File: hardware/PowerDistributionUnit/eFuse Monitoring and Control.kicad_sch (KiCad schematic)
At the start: 103 parts, among them U34 MCP23017_SO, U37 MCP23017_SO, U38 ADS131M08-Q1, U39 ADS131M08-Q1, Y1 ABM3-8.000MHZ-D2Y-T

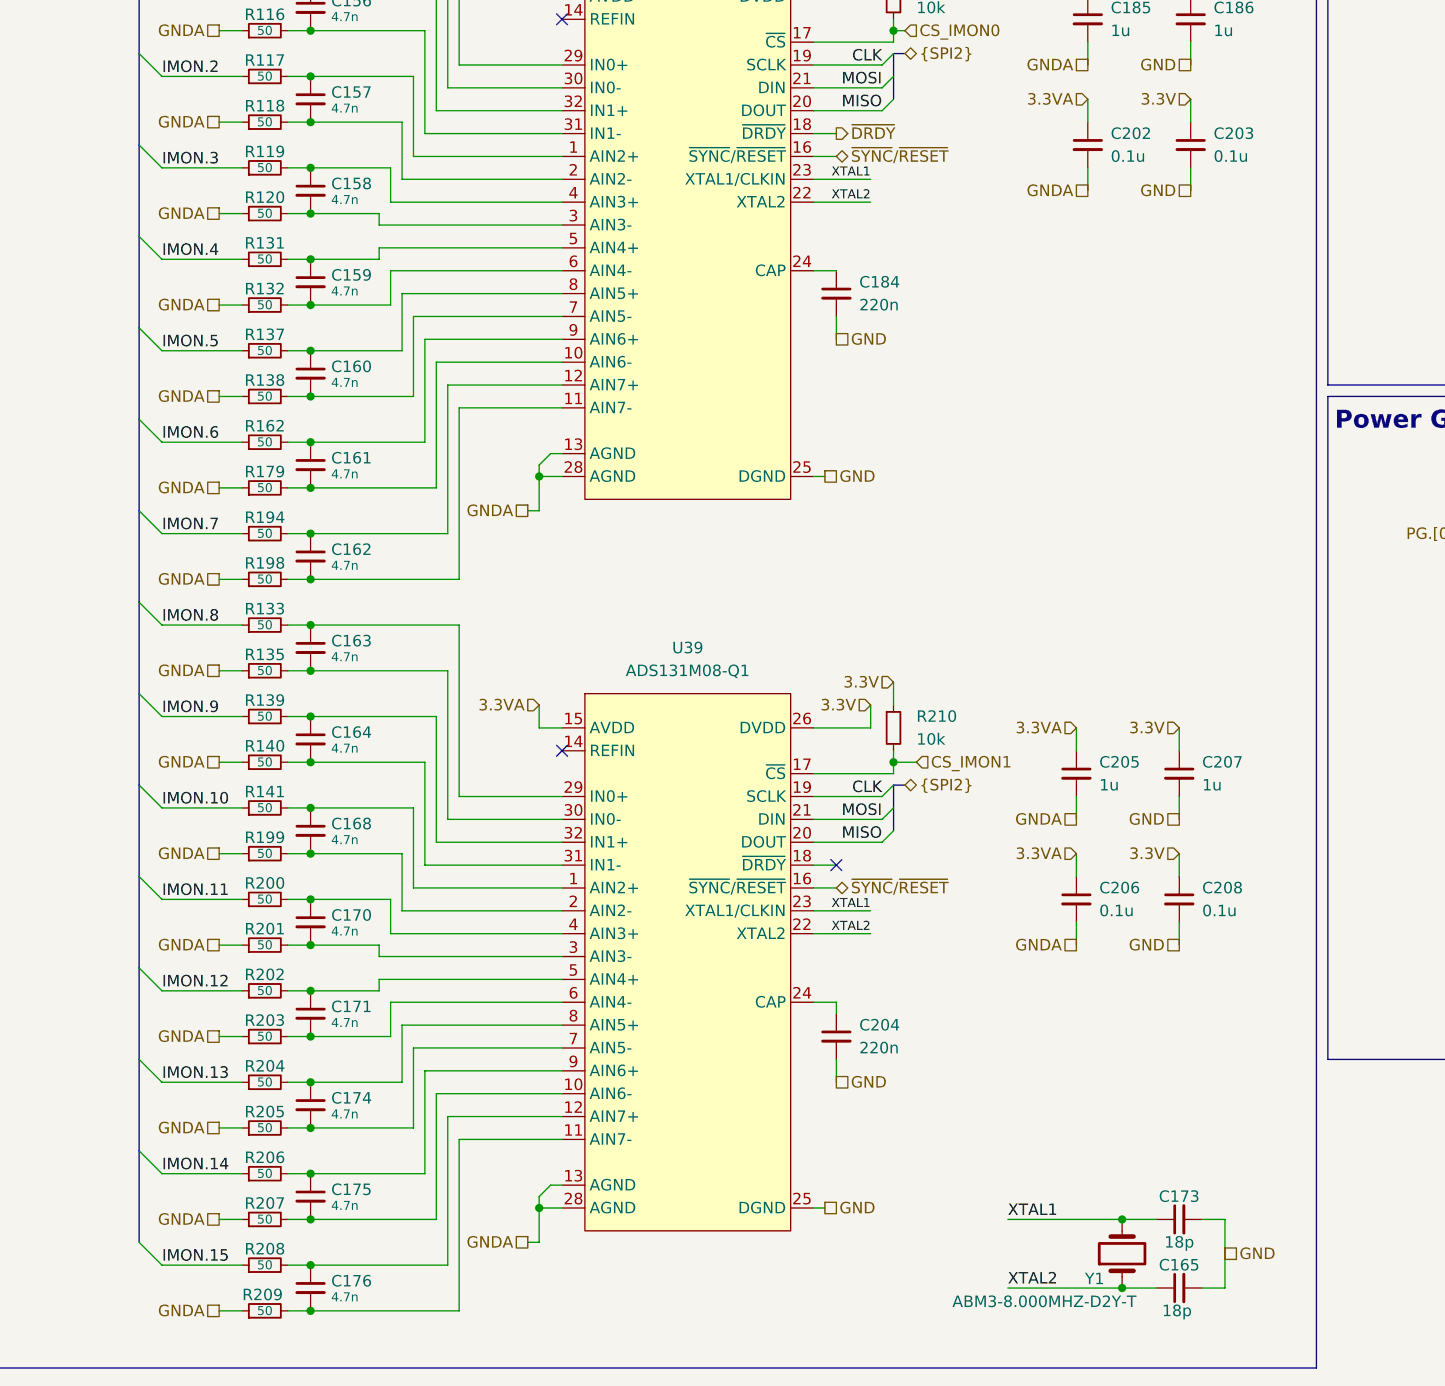
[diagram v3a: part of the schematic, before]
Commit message: updated adc, preliminary routing plan
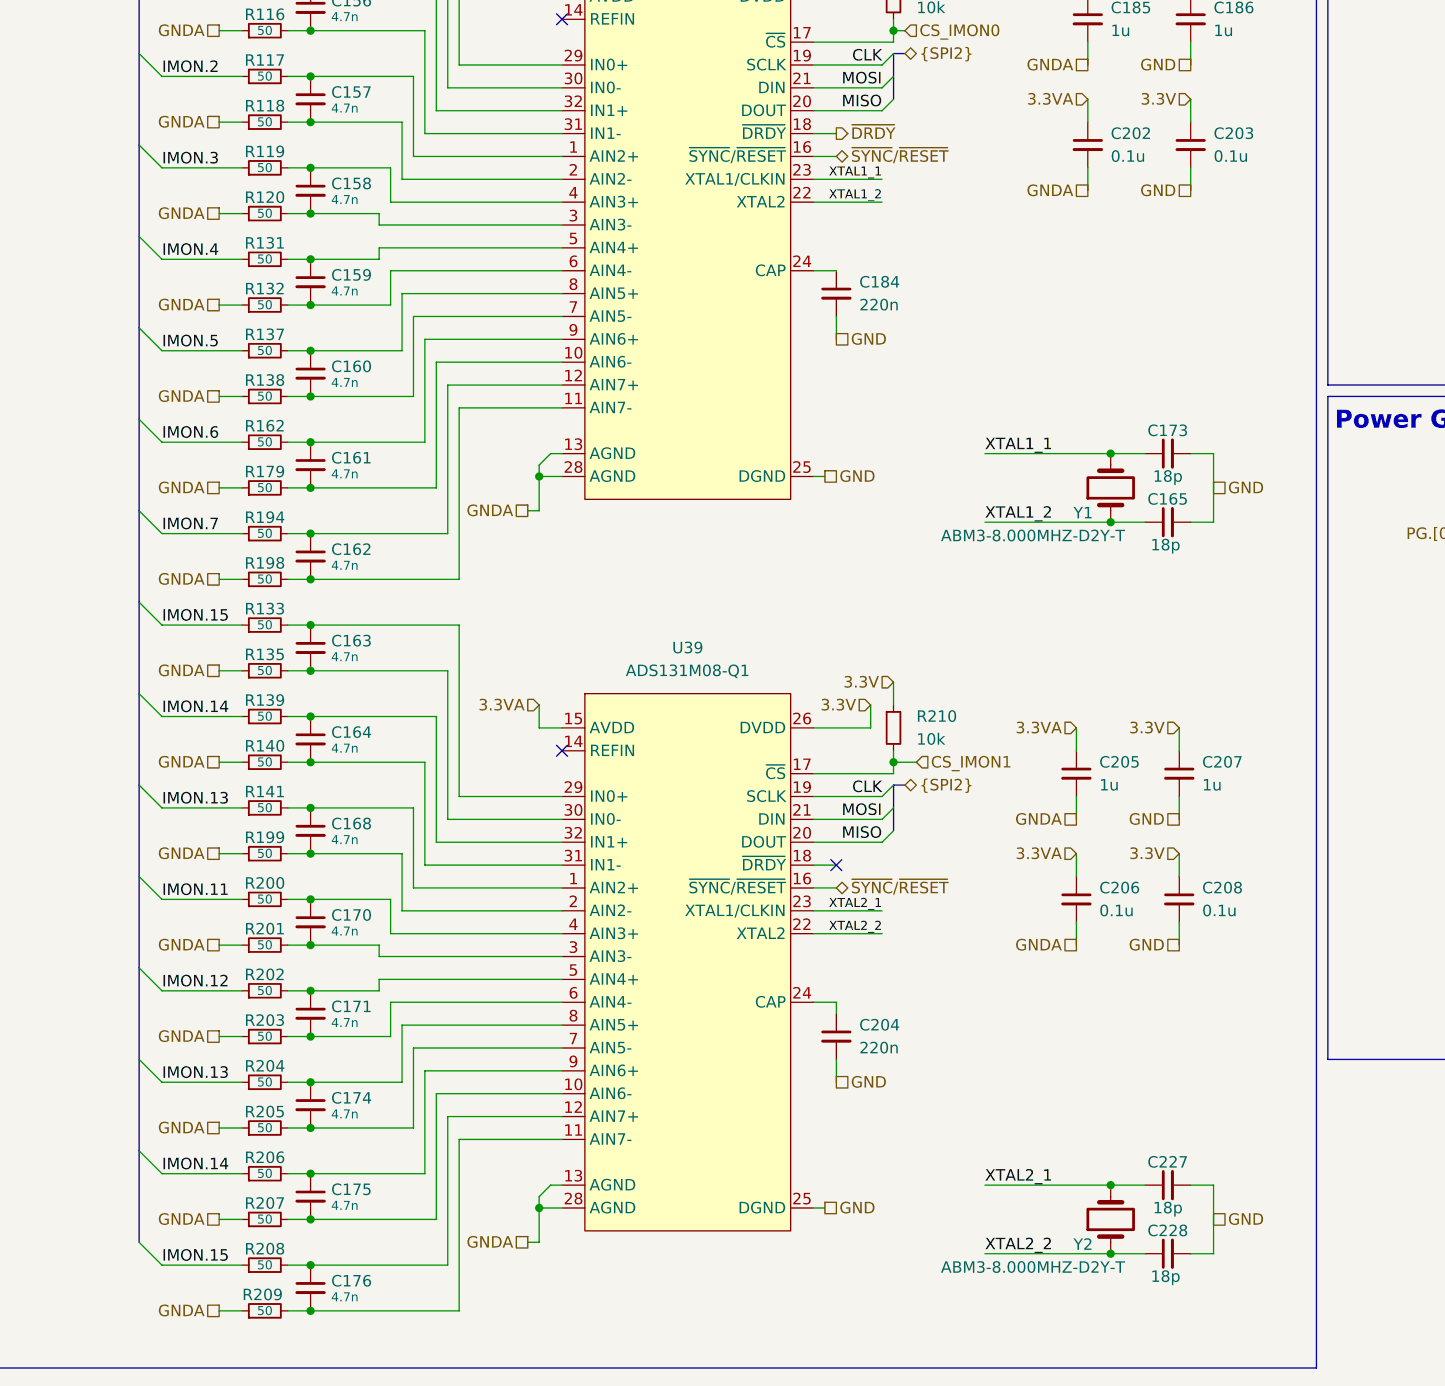
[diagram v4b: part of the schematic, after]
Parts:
- added C227, C228: 18p, Capacitor_SMD:C_0603_1608Metric, symbol Device:C_Small
- added Y2: ABM3-8.000MHZ-D2Y-T, PowerDistributionUnitLib:ABM3, symbol Device:Crystal
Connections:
- net IMON.10 is gone; now on net IMON.13: R141.1
- net IMON.8 is gone; now on net IMON.15: R133.1
- net IMON.9 is gone; now on net IMON.14: R139.1
- net GND: now also C227.2, C228.2
- net XTAL1 renamed XTAL1_1
- net XTAL1_1: no longer U39.23 (XTAL1/CLKIN)
- net XTAL2 renamed XTAL1_2
- net XTAL1_2: no longer U39.22 (XTAL2)
- new net XTAL2_1: C227.1, U39.23 (XTAL1/CLKIN), Y2.2
- new net XTAL2_2: C228.1, U39.22 (XTAL2), Y2.1
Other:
- moved on the sheet: C165, C173, Y1

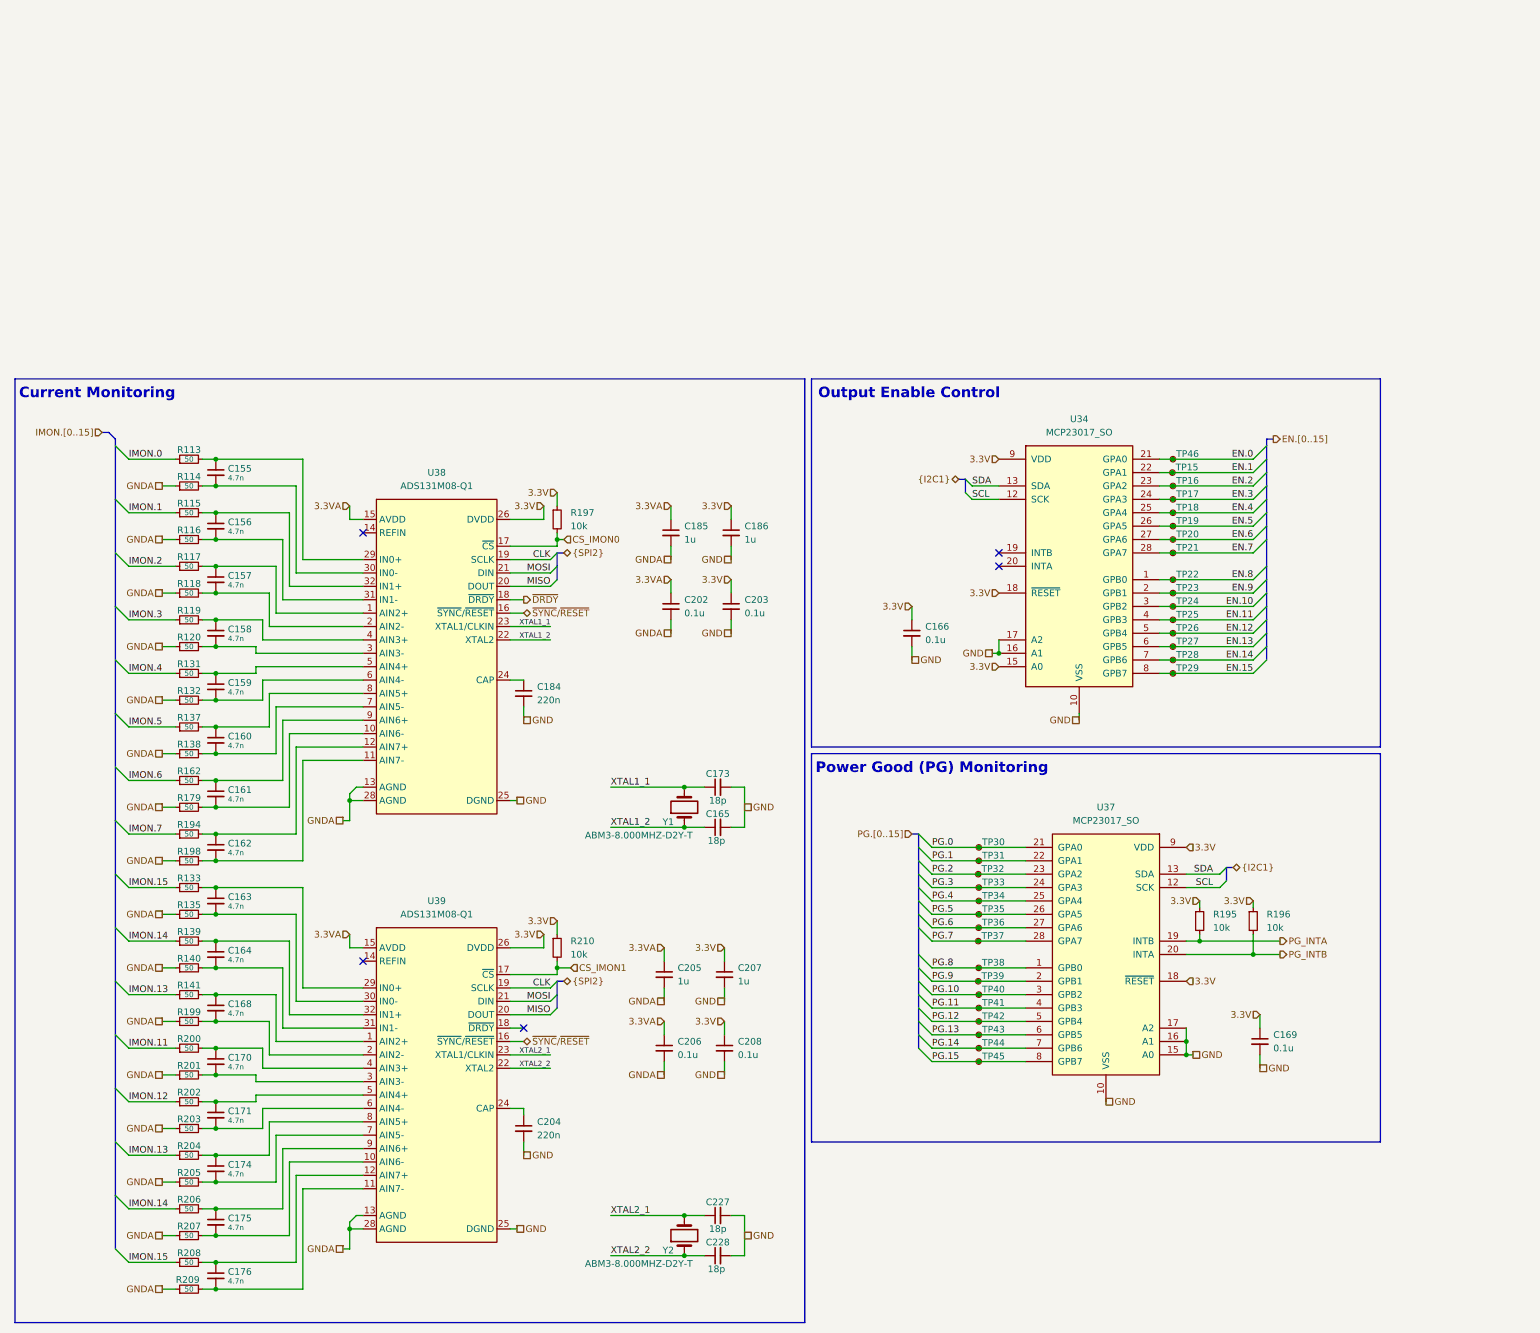
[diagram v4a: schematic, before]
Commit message: routed ADCs for IMON
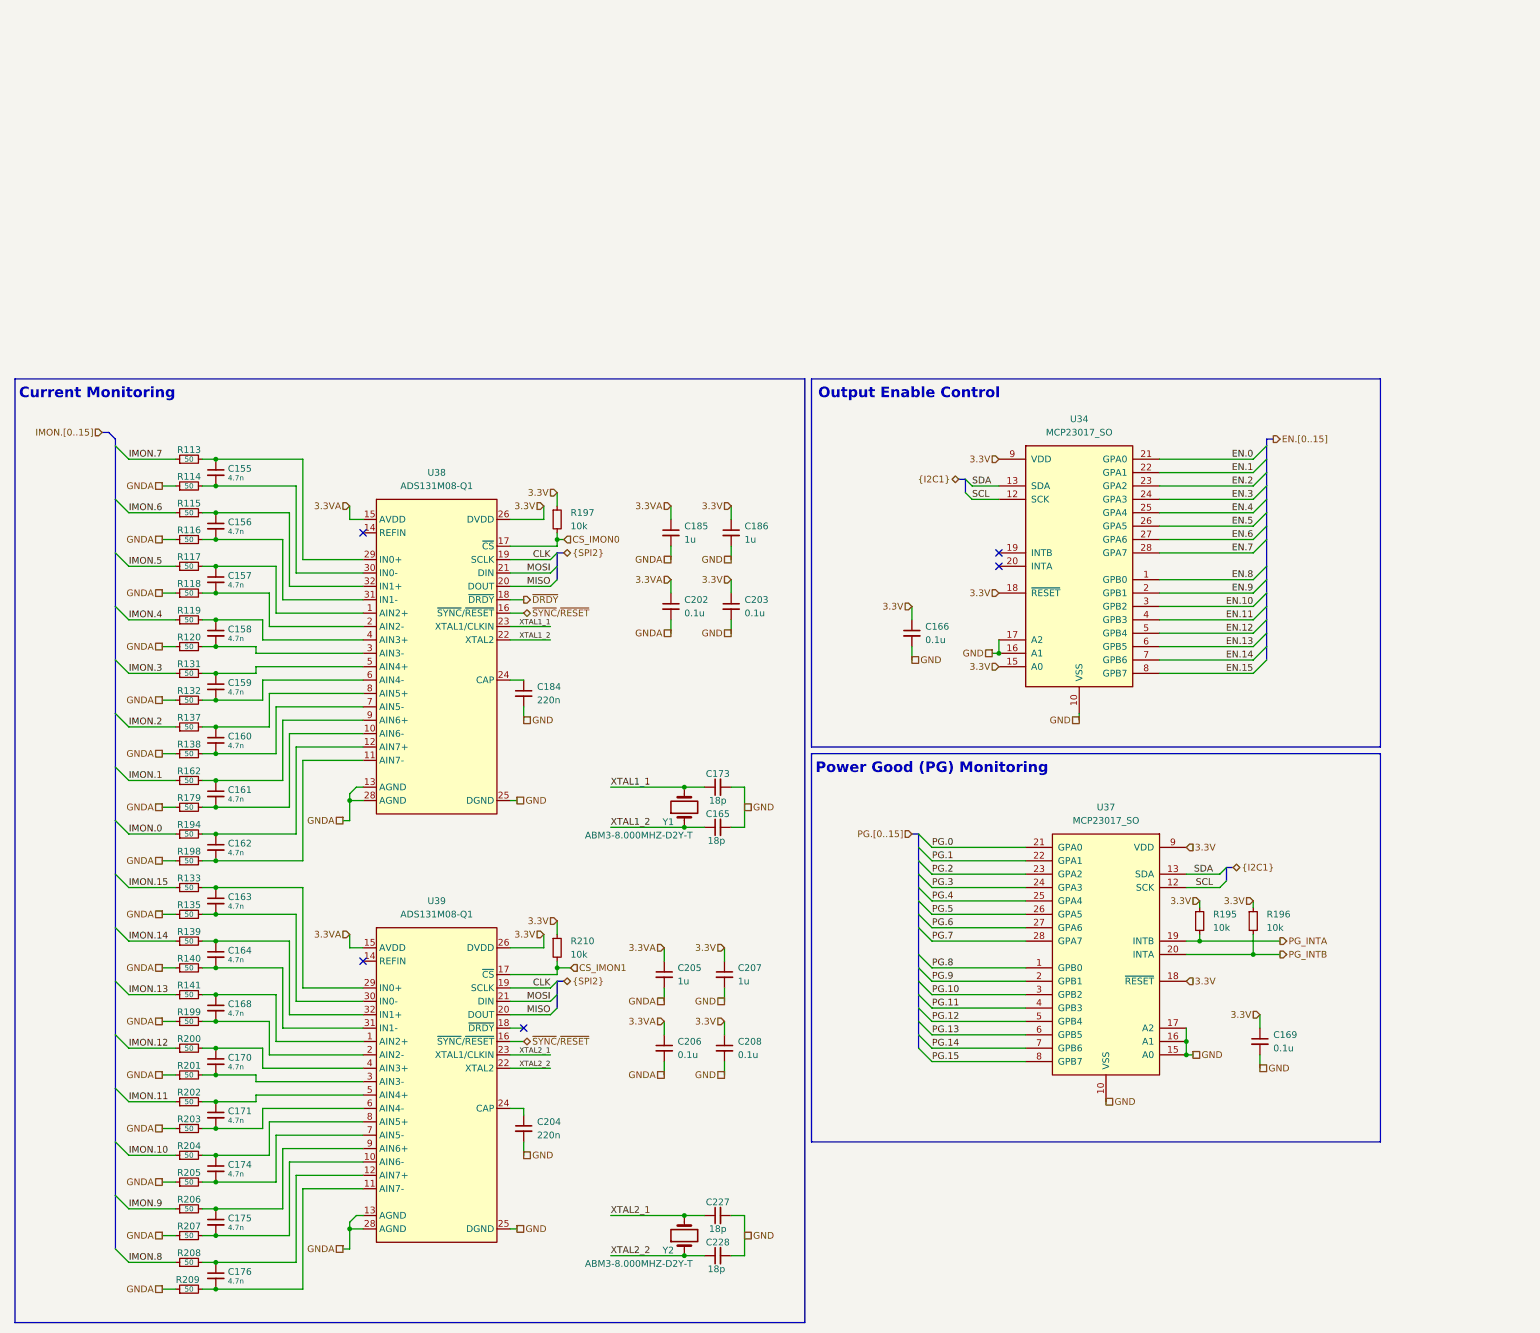
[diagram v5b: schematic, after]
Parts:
- removed TP15, TP16, TP17, TP18, TP19, TP20, TP21, TP22, TP23, TP24, TP25, TP26, TP27, TP28, TP29, TP30, TP31, TP32, TP33, TP34, TP35, TP36, TP37, TP38, TP39, TP40, TP41, TP42, TP43, TP44, TP45, TP46: TestPoint_Small, TestPoint:TestPoint_Pad_D1.0mm, symbol Connector:TestPoint_Small
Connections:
- net IMON.0: now also R194.1; no longer R113.1
- net IMON.1: now also R162.1; no longer R115.1
- net IMON.11: now also R202.1; no longer R200.1
- net IMON.12: now also R200.1; no longer R202.1
- net IMON.13: no longer R204.1
- net IMON.14: no longer R206.1
- net IMON.15: no longer R208.1
- net IMON.2: now also R137.1; no longer R117.1
- net IMON.3: now also R131.1; no longer R119.1
- net IMON.4: now also R119.1; no longer R131.1
- net IMON.5: now also R117.1; no longer R137.1
- net IMON.6: now also R115.1; no longer R162.1
- net IMON.7: now also R113.1; no longer R194.1
- new net IMON.10: R204.1
- new net IMON.8: R208.1
- new net IMON.9: R206.1
